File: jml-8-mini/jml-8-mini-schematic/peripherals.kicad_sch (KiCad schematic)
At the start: 9 parts, among them J2 SIO CHB, J3 UART, J4 CTC Extra Lines, U4 Z80CTC, U5 Z80SIO

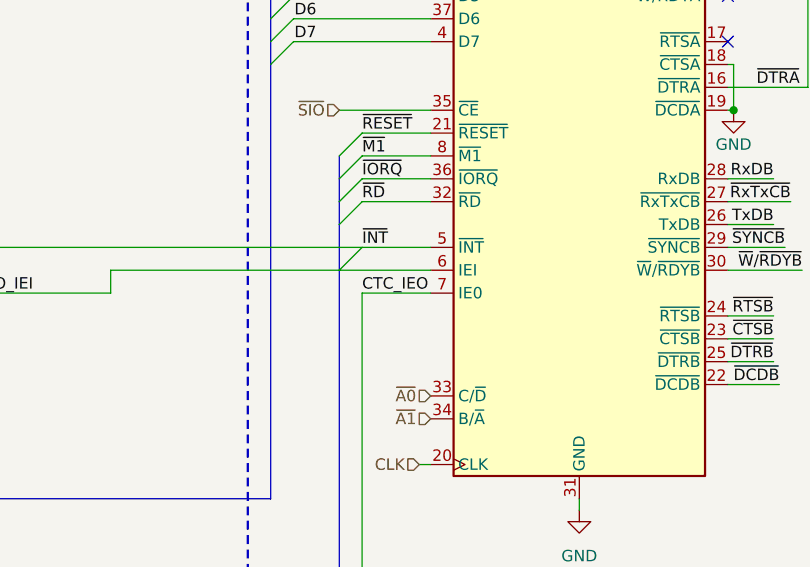
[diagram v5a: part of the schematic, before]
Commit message: fix wrong label, add labels and figures to pcb
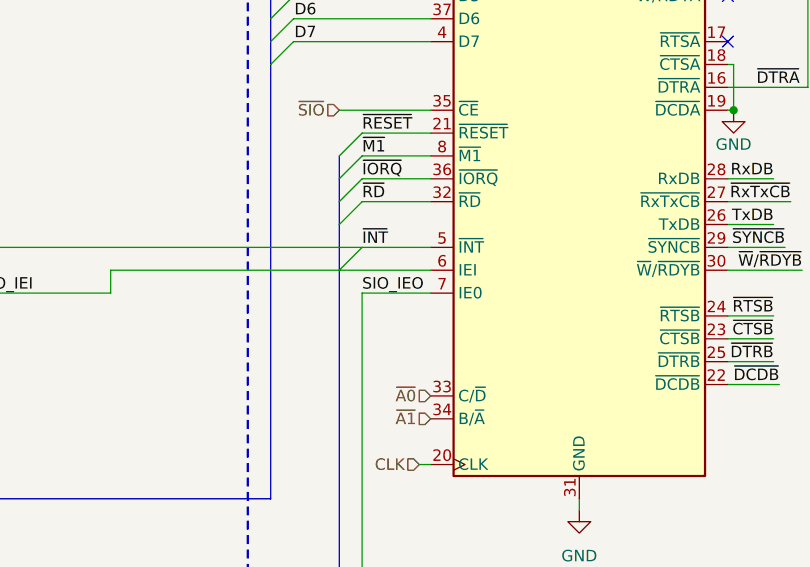
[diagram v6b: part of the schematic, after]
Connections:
- net CTC_IEO renamed SIO_IEO
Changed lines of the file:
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@@
     (effects (font (size 1.27 1.27)) (justify left bottom))
   )
-  (label "CTC_IEO" (at 194.31 84.455 0) (fields_autoplaced)
+  (label "SIO_IEO" (at 194.31 84.455 0) (fields_autoplaced)
     (effects (font (size 1.27 1.27)) (justify left bottom))
   )
